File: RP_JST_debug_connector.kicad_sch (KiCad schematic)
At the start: 0 parts

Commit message: Downloaded the Footprints for RP2350B
Downloaded the ABM8-272-T3 for the crystal and the SM03B-SRSS-TB for the JST connector, though the later is not correct (I think) because it lacks mechanical pads within the footprint.
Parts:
- added J4: SM03B-SRSS-TB, CONN_SM03B-SRSS-TB_JST, symbol SM03B-SRSS-TB:SM03B-SRSS-TB
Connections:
- new net GND: J4.2
- new net SWCLK: J4.1
- new net SWD: J4.3
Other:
- note added: "<-- Should be an MP here"
- note added: "This doesn't seem to match, but I'm going to save this for now and get back to it later. There should be an MP where wire connects to nowhere on the SM03B."
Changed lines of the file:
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@@
 	(generator_version "9.0")
 	(paper "A4")
+	(text "<-- Should be an MP here"
+		(exclude_from_sim no)
+		(at 154.94 110.49 0)
+		(effects
+			(font
+				(size 1.27 1.27)
+			)
+		)
+	)
+	(text "This doesn't seem to match, but I'm going to save this for now\nand get back to it later.\nThere should be an MP where wire connects to nowhere on the SM03B."
+		(exclude_from_sim no)
+		(at 139.7 95.25 0)
+		(effects
+			(font
+				(size 1.27 1.27)
+			)
+		)
+	)
+	(junction
+		(at 128.27 119.38)
+		(diameter 0)
+		(color 0 0 0 0)
+	)
+	(wire
+		(pts
+			(xy 128.27 119.38) (xy 128.27 121.92)
+		)
+		(stroke
+			(width 0)
+			(type default)
+		)
+	)
+	(wire
+		(pts
+			(xy 132.08 104.14) (xy 128.27 104.14)
+		)
+		(stroke
+			(width 0)
+			(type default)
+		)
+	)
+	(wire
+		(pts
+			(xy 120.65 101.6) (xy 132.08 101.6)
+		)
+		(stroke
+			(width 0)
+			(type default)
+		)
+	)
+	(wire
+		(pts
+			(xy 128.27 104.14) (xy 128.27 119.38)
+		)
+		(stroke
+			(width 0)
+			(type default)
+		)
+	)
+	(wire
+		(pts
+			(xy 140.97 109.22) (xy 140.97 119.38)
+		)
+		(stroke
+			(width 0)
+			(type default)
+		)
+	)
+	(wire
+		(pts
+			(xy 128.27 119.38) (xy 140.97 119.38)
+		)
+		(stroke
+			(width 0)
+			(type default)
+		)
+	)
+	(wire
+		(pts
+			(xy 120.65 106.68) (xy 132.08 106.68)
+		)
+		(stroke
+			(width 0)
+			(type default)
+		)
+	)
+	(label "SWCLK"
+		(at 120.65 101.6 0)
+		(effects
+			(font
+				(size 1.27 1.27)
+			)
+			(justify left bottom)
+		)
+	)
+	(label "SWD"
+		(at 120.65 106.68 0)
+		(effects
+			(font
+				(size 1.27 1.27)
+			)
+			(justify left bottom)
+		)
+	)
+	(symbol
+		(lib_id "SM03B-SRSS-TB:SM03B-SRSS-TB")
+		(at 132.08 101.6 0)
+		(unit 1)
+		(exclude_from_sim no)
+		(in_bom yes)
+		(on_board yes)
+		(dnp no)
+		(fields_autoplaced yes)
+		(property "Reference" "J4"
+			(at 146.05 102.8699 0)
+			(effects
+				(font
+					(size 1.524 1.524)
+				)
+				(justify left)
+			)
+		)
+		(property "Value" "SM03B-SRSS-TB"
+			(at 146.05 105.4099 0)
+			(effects
+				(font
+					(size 1.524 1.524)
+				)
+				(justify left)
+			)
+		)
+		(property "Footprint" "CONN_SM03B-SRSS-TB_JST"
+			(at 132.08 101.6 0)
+			(effects
+				(font
+					(size 1.27 1.27)
+					(italic yes)
+				)
+				(hide yes)
+			)
+		)
+		(property "Datasheet" "SM03B-SRSS-TB"
+			(at 132.08 101.6 0)
+			(effects
+				(font
+					(size 1.27 1.27)
+					(italic yes)
+				)
+				(hide yes)
+			)
+		)
+		(property "Description" ""
+			(at 132.08 101.6 0)
+			(effects
+				(font
+					(size 1.27 1.27)
+				)
+				(hide yes)
+			)
+		)
+		(pin "1"
+		)
+		(pin "3"
+		)
+		(pin "2"
+		)
+		(instances
+			(project ""
+				(path "/31ba118e-63c6-4589-abeb-d0c379bb13c1/c6c9b9a9-ddbf-445b-97cd-a6e878077684/266ce9e5-2999-4c85-a3f1-1dd81239aec3"
+					(reference "J4")
+					(unit 1)
+				)
+			)
+		)
+	)
+	(symbol
+		(lib_id "power:GND")
+		(at 128.27 121.92 0)
+		(unit 1)
+		(exclude_from_sim no)
+		(in_bom yes)
+		(on_board yes)
+		(dnp no)
+		(fields_autoplaced yes)
+		(property "Reference" "#PWR030"
+			(at 128.27 128.27 0)
+			(effects
+				(font
+					(size 1.27 1.27)
+				)
+				(hide yes)
+			)
+		)
+		(property "Value" "GND"
+			(at 128.27 127 0)
+			(effects
+				(font
+					(size 1.27 1.27)
+				)
+			)
+		)
+		(property "Footprint" ""
+			(at 128.27 121.92 0)
+			(effects
+				(font
+					(size 1.27 1.27)
+				)
+				(hide yes)
+			)
+		)
+		(property "Datasheet" ""
+			(at 128.27 121.92 0)
+			(effects
+				(font
+					(size 1.27 1.27)
+				)
+				(hide yes)
+			)
+		)
+		(property "Description" "Power symbol creates a global label with name \"GND\" , ground"
+			(at 128.27 121.92 0)
+			(effects
+				(font
+					(size 1.27 1.27)
+				)
+				(hide yes)
+			)
+		)
+		(pin "1"
+		)
+		(instances
+			(project ""
+				(path "/31ba118e-63c6-4589-abeb-d0c379bb13c1/c6c9b9a9-ddbf-445b-97cd-a6e878077684/266ce9e5-2999-4c85-a3f1-1dd81239aec3"
+					(reference "#PWR030")
+					(unit 1)
+				)
+			)
+		)
+	)
 )

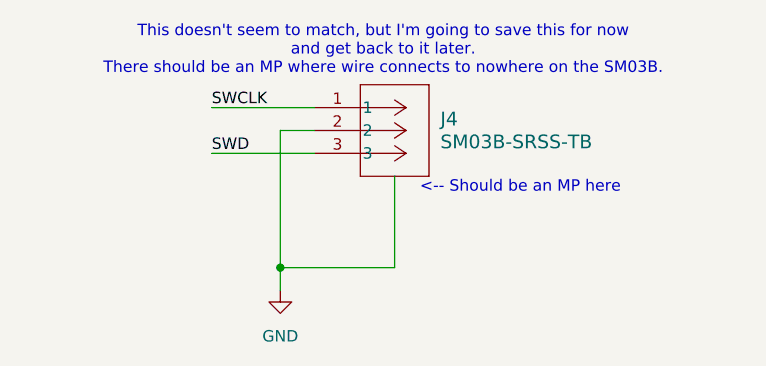
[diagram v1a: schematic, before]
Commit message: Consolidate/mostly finalize avionics
Add RP2350 components to same sheet as RP2350, replace flash with MRAM
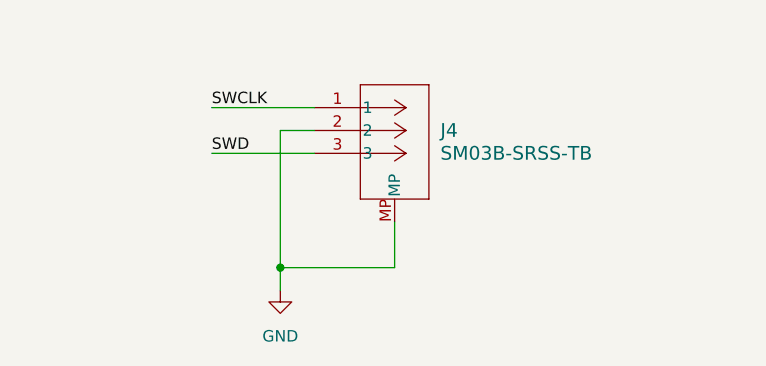
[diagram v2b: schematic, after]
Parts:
- removed J4: SM03B-SRSS-TB, CONN_SM03B-SRSS-TB_JST, symbol SM03B-SRSS-TB:SM03B-SRSS-TB
- added J4: SM03B-SRSS-TB, CONN_SM03B-SRSS-TB_JST, symbol 2025-12-23_04-50-52:SM03B-SRSS-TB
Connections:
- net GND: now also J4.2, J4.MP
- net SWCLK: now also J4.1
- net SWD: now also J4.3
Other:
- note removed: "<-- Should be an MP here"
- note removed: "This doesn't seem to match, but I'm going to save this for now and get back to it later. There should be an MP where wire connects to nowhere on the SM03B."
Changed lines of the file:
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@@
 	(generator_version "9.0")
 	(paper "A4")
-	(text "<-- Should be an MP here"
-		(exclude_from_sim no)
-		(at 154.94 110.49 0)
-		(effects
-			(font
-				(size 1.27 1.27)
-			)
-		)
-	)
-	(text "This doesn't seem to match, but I'm going to save this for now\nand get back to it later.\nThere should be an MP where wire connects to nowhere on the SM03B."
-		(exclude_from_sim no)
-		(at 139.7 95.25 0)
-		(effects
-			(font
-				(size 1.27 1.27)
-			)
-		)
-	)
 	(junction
 		(at 128.27 119.38)
@@
 	(wire
 		(pts
+			(xy 120.65 101.6) (xy 132.08 101.6)
+		)
+		(stroke
+			(width 0)
+			(type default)
+		)
+	)
+	(wire
+		(pts
+			(xy 120.65 106.68) (xy 132.08 106.68)
+		)
+		(stroke
+			(width 0)
+			(type default)
+		)
+	)
+	(wire
+		(pts
 			(xy 132.08 104.14) (xy 128.27 104.14)
 		)
@@
 	(wire
 		(pts
-			(xy 120.65 101.6) (xy 132.08 101.6)
-		)
-		(stroke
-			(width 0)
-			(type default)
-		)
-	)
-	(wire
-		(pts
 			(xy 128.27 104.14) (xy 128.27 119.38)
 		)
@@
 	(wire
 		(pts
-			(xy 140.97 109.22) (xy 140.97 119.38)
+			(xy 140.97 114.3) (xy 140.97 119.38)
 		)
 		(stroke
@@
 		(pts
 			(xy 128.27 119.38) (xy 140.97 119.38)
-		)
-		(stroke
-			(width 0)
-			(type default)
-		)
-	)
-	(wire
-		(pts
-			(xy 120.65 106.68) (xy 132.08 106.68)
 		)
 		(stroke
@@
 			)
 			(justify left bottom)
-		)
-	)
-	(symbol
-		(lib_id "SM03B-SRSS-TB:SM03B-SRSS-TB")
-		(at 132.08 101.6 0)
-		(unit 1)
-		(exclude_from_sim no)
-		(in_bom yes)
-		(on_board yes)
-		(dnp no)
-		(fields_autoplaced yes)
-		(property "Reference" "J4"
-			(at 146.05 102.8699 0)
-			(effects
-				(font
-					(size 1.524 1.524)
-				)
-				(justify left)
-			)
-		)
-		(property "Value" "SM03B-SRSS-TB"
-			(at 146.05 105.4099 0)
-			(effects
-				(font
-					(size 1.524 1.524)
-				)
-				(justify left)
-			)
-		)
-		(property "Footprint" "CONN_SM03B-SRSS-TB_JST"
-			(at 132.08 101.6 0)
-			(effects
-				(font
-					(size 1.27 1.27)
-					(italic yes)
-				)
-				(hide yes)
-			)
-		)
-		(property "Datasheet" "SM03B-SRSS-TB"
-			(at 132.08 101.6 0)
-			(effects
-				(font
-					(size 1.27 1.27)
-					(italic yes)
-				)
-				(hide yes)
-			)
-		)
-		(property "Description" ""
-			(at 132.08 101.6 0)
-			(effects
-				(font
-					(size 1.27 1.27)
-				)
-				(hide yes)
-			)
-		)
-		(pin "1"
-		)
-		(pin "3"
-		)
-		(pin "2"
-		)
-		(instances
-			(project ""
-				(path "/31ba118e-63c6-4589-abeb-d0c379bb13c1/c6c9b9a9-ddbf-445b-97cd-a6e878077684/266ce9e5-2999-4c85-a3f1-1dd81239aec3"
-					(reference "J4")
-					(unit 1)
-				)
-			)
 		)
 	)
@@
 					(unit 1)
 				)
+			)
+		)
+	)
+	(symbol
+		(lib_id "2025-12-23_04-50-52:SM03B-SRSS-TB")
+		(at 132.08 101.6 0)
+		(unit 1)
+		(exclude_from_sim no)
+		(in_bom yes)
+		(on_board yes)
+		(dnp no)
+		(fields_autoplaced yes)
+		(property "Reference" "J4"
+			(at 146.05 104.1399 0)
+			(effects
+				(font
+					(size 1.524 1.524)
+				)
+				(justify left)
+			)
+		)
+		(property "Value" "SM03B-SRSS-TB"
+			(at 146.05 106.6799 0)
+			(effects
+				(font
+					(size 1.524 1.524)
+				)
+				(justify left)
+			)
+		)
+		(property "Footprint" "CONN_SM03B-SRSS-TB_JST"
+			(at 131.064 97.79 0)
+			(effects
+				(font
+					(size 1.27 1.27)
+					(italic yes)
+				)
+				(hide yes)
+			)
+		)
+		(property "Datasheet" "SM03B-SRSS-TB"
+			(at 132.08 101.6 0)
+			(effects
+				(font
+					(size 1.27 1.27)
+					(italic yes)
+				)
+				(hide yes)
+			)
+		)
+		(property "Description" ""
+			(at 132.08 101.6 0)
+			(effects
+				(font
+					(size 1.27 1.27)
+				)
+				(hide yes)
+			)
+		)
+		(pin "3"
+		)
+		(pin "MP"
+		)
+		(pin "2"
+		)
+		(pin "1"
+		)
+		(instances
+			(project ""
+				(path "/31ba118e-63c6-4589-abeb-d0c379bb13c1/c6c9b9a9-ddbf-445b-97cd-a6e878077684/266ce9e5-2999-4c85-a3f1-1dd81239aec3"
+					(reference "J4")
+					(unit 1)
+				)
